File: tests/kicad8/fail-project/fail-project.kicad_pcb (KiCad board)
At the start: 2 copper layers, 45.7 x 21.6 mm, 6 parts, among them P1 CONN_01X02

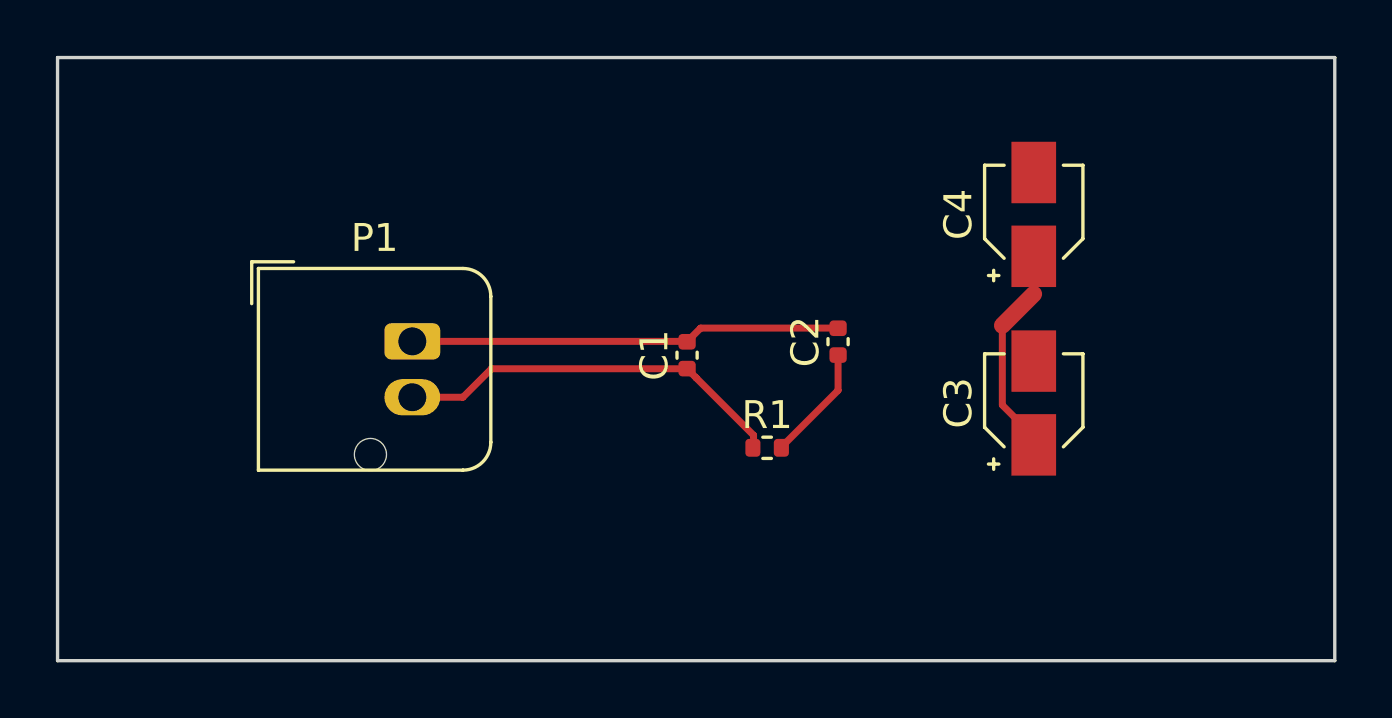
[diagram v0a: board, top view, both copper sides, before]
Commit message: [PCBNew][DRC] Implemented CLI version
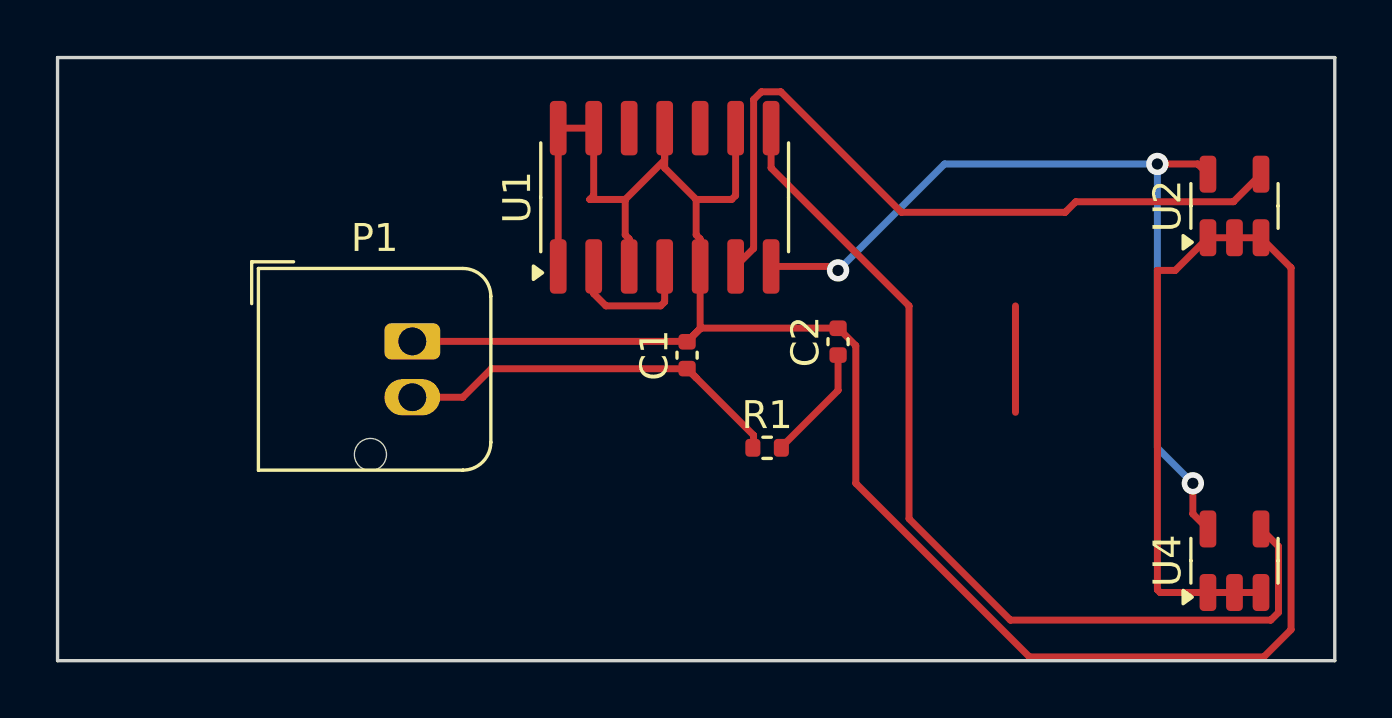
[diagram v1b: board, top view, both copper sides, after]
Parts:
- removed C3, C4: CP, Capacitor_SMD:CP_Elec_3x5.3
- added U1: 74LS04, Package_SO:SOIC-14_3.9x8.7mm_P1.27mm, F.Cu at (164.0, 74.9)
- added U2: 74AHC1G126, Package_TO_SOT_SMD:SOT-23-5, F.Cu at (184.4, 75.2)
- added U4: 74AHC1G126, Package_TO_SOT_SMD:SOT-23-5, F.Cu at (184.4, 87.9)
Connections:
- net /Power/VCC renamed VCC
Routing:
- net GND: track 15.4 -> 101.6 mm
- net Net-(U1-Pad8): track 0.00 -> 34.1 mm
- net VCC: track 14.1 -> 45.8 mm, vias 0 -> 3
- net Net-(U1-Pad6): track 0.00 -> 26.9 mm
- net Net-(C3-Pad1): track 7.68 -> 0.00 mm
- net Net-(U1-Pad2): track 0.00 -> 5.03 mm
- net (no net): track 0.00 -> 3.81 mm
